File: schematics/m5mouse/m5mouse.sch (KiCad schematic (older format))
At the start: 52 parts, among them IC1 LM3940IMP-3.3_NOPB, J1 Conn_01x02, J2 M-BUS, J3 SWD, J6 Conn_01x03, J7 Conn_01x06, J8 Conn_01x06, SW1 SW_SPDT, SW2 SW_Push, U1 TPS562200, U2 STM32F405RGTx, Y1 8MHz, Y2 32.768kHz

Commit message: Fix path
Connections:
- net GND: no longer C15.1, C16.1, C17.1, U2.12 (VSSA)
- net GPIO10: now also U2.50 (PA15); no longer U2.34 (PB13)
- new net GNDA: C15.1, C16.1, C17.1, U2.12 (VSSA)
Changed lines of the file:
@@
 Wire Wire Line
 	12200 7200 12200 7300
-Wire Wire Line
-	12200 7300 12300 7300
-Wire Wire Line
-	12300 7300 12300 7200
-Wire Wire Line
-	12300 7300 12400 7300
-Wire Wire Line
-	12400 7300 12400 7200
-Connection ~ 12300 7300
-Wire Wire Line
-	12300 7300 12300 7400
 $Comp
 L Device:C C11
@@
 	13450 3100 13450 3200
 Connection ~ 13150 3100
-$Comp
-L power:GND #PWR0108
-U 1 1 5EECB65E
-P 13850 3200
-F 0 "#PWR0108" H 13850 2950 50  0001 C CNN
-F 1 "GND" H 13855 3027 50  0000 C CNN
-F 2 "" H 13850 3200 50  0001 C CNN
-F 3 "" H 13850 3200 50  0001 C CNN
-	1    13850 3200
-	1    0    0    -1
-$EndComp
 Wire Wire Line
 	13450 3100 13850 3100
@@
 Text GLabel 13250 5600 2    50   Output ~ 0
 GPIO3
-Text GLabel 9550 9400 0    50   Input ~ 0
+Text GLabel 9550 9100 0    50   Input ~ 0
 GPIO5
-Text GLabel 9550 9250 0    50   Input ~ 0
+Text GLabel 9550 8950 0    50   Input ~ 0
 GPIO4
-Text GLabel 9550 9100 0    50   Input ~ 0
+Text GLabel 9550 9400 0    50   Input ~ 0
 GPIO3
-Text GLabel 9550 8950 0    50   Input ~ 0
+Text GLabel 9550 9250 0    50   Input ~ 0
 GPIO2
 Text GLabel 11500 8950 2    50   Output ~ 0
@@
 Wire Wire Line
 	9350 2300 9350 2250
-Text GLabel 13250 6800 2    50   Output ~ 0
+Text GLabel 13250 5300 2    50   Output ~ 0
 GPIO10
 Text GLabel 9550 6750 2    50   Input ~ 0
@@
 Wire Wire Line
 	13000 6700 13250 6700
-Wire Wire Line
-	13250 6800 13000 6800
-$Comp
-L power:GNDA #PWR028
-U 1 1 5F5519D3
-P 12300 7500
-F 0 "#PWR028" H 12300 7250 50  0001 C CNN
-F 1 "GNDA" H 12305 7327 50  0000 C CNN
-F 2 "" H 12300 7500 50  0001 C CNN
-F 3 "" H 12300 7500 50  0001 C CNN
-	1    12300 7500
-	1    0    0    -1
-$EndComp
-$Comp
-L power:GND #PWR027
-U 1 1 5F551FD9
-P 11900 7500
-F 0 "#PWR027" H 11900 7250 50  0001 C CNN
-F 1 "GND" H 11905 7327 50  0000 C CNN
-F 2 "" H 11900 7500 50  0001 C CNN
-F 3 "" H 11900 7500 50  0001 C CNN
-	1    11900 7500
-	1    0    0    -1
-$EndComp
-Wire Wire Line
-	11900 7500 11900 7400
-Wire Wire Line
-	11900 7400 12300 7400
-Connection ~ 12300 7400
-Wire Wire Line
-	12300 7400 12300 7500
 $Sheet
 S 13400 7850 1050 650
@@
 Text GLabel 13250 4200 2    50   Output ~ 0
 GPIO11
-NoConn ~ 13000 5300
+NoConn ~ 13000 6800
 Text GLabel 11350 6700 0    50   Output ~ 0
 SPI1_CS
@@
 	14200 3600 15000 3600
 NoConn ~ 11600 6600
+Wire Wire Line
+	12300 7200 12300 7300
+Wire Wire Line
+	12300 7300 12200 7300
+$Comp
+L power:GNDA #PWR0108
+U 1 1 5F55198E
+P 13850 3200
+F 0 "#PWR0108" H 13850 2950 50  0001 C CNN
+F 1 "GNDA" H 13855 3027 50  0000 C CNN
+F 2 "" H 13850 3200 50  0001 C CNN
+F 3 "" H 13850 3200 50  0001 C CNN
+	1    13850 3200
+	1    0    0    -1
+$EndComp
+$Comp
+L power:GNDA #PWR028
+U 1 1 5F5519D3
+P 12400 7500
+F 0 "#PWR028" H 12400 7250 50  0001 C CNN
+F 1 "GNDA" H 12405 7327 50  0000 C CNN
+F 2 "" H 12400 7500 50  0001 C CNN
+F 3 "" H 12400 7500 50  0001 C CNN
+	1    12400 7500
+	1    0    0    -1
+$EndComp
+Connection ~ 12200 7300
+$Comp
+L power:GND #PWR027
+U 1 1 5F551FD9
+P 11900 7500
+F 0 "#PWR027" H 11900 7250 50  0001 C CNN
+F 1 "GND" H 11905 7327 50  0000 C CNN
+F 2 "" H 11900 7500 50  0001 C CNN
+F 3 "" H 11900 7500 50  0001 C CNN
+	1    11900 7500
+	1    0    0    -1
+$EndComp
+Wire Wire Line
+	11900 7300 11900 7500
+Wire Wire Line
+	12200 7300 11900 7300
+Wire Wire Line
+	12400 7200 12400 7500
+$Comp
+L power:GNDA #PWR0136
+U 1 1 5F651608
+P 3500 1350
+F 0 "#PWR0136" H 3500 1100 50  0001 C CNN
+F 1 "GNDA" H 3505 1177 50  0000 C CNN
+F 2 "" H 3500 1350 50  0001 C CNN
+F 3 "" H 3500 1350 50  0001 C CNN
+	1    3500 1350
+	1    0    0    -1
+$EndComp
+$Comp
+L power:PWR_FLAG #FLG0103
+U 1 1 5F666704
+P 3500 1150
+F 0 "#FLG0103" H 3500 1225 50  0001 C CNN
+F 1 "PWR_FLAG" H 3500 1323 50  0000 C CNN
+F 2 "" H 3500 1150 50  0001 C CNN
+F 3 "~" H 3500 1150 50  0001 C CNN
+	1    3500 1150
+	1    0    0    -1
+$EndComp
+Wire Wire Line
+	3500 1150 3500 1350
+Wire Wire Line
+	13000 5300 13250 5300
 $EndSCHEMATC

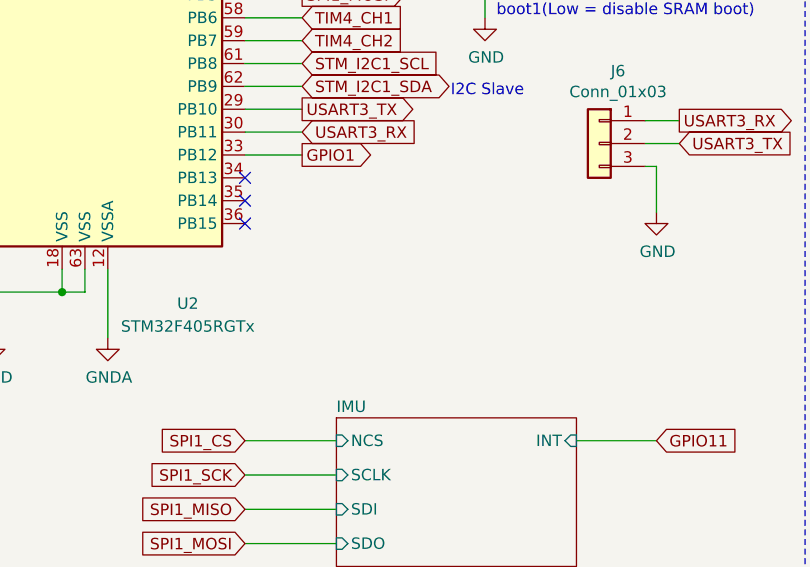
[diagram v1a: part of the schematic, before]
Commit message: Connect GNDA and GND via ferrite bead
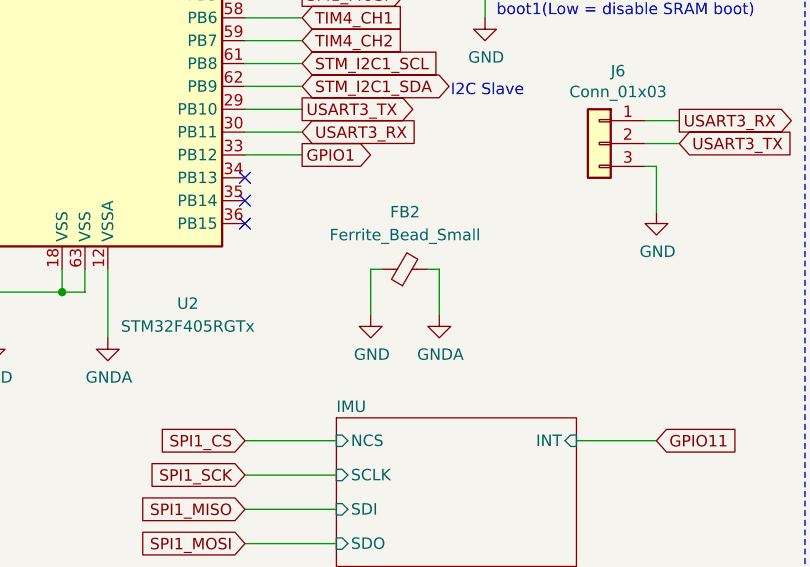
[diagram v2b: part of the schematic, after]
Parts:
- added FB2: Ferrite_Bead_Small, Resistor_SMD:R_0603_1608Metric, symbol Device:Ferrite_Bead_Small
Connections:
- net GND: now also FB2.1
- net GNDA: now also FB2.2
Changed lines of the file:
@@
 	1550 4650 1600 4650
 $Comp
-L MCU_ST_STM32F4:STM32F405RGTx U2
-U 1 1 5ED1928B
-P 12300 5400
-F 0 "U2" H 12750 3450 50  0000 C CNN
-F 1 "STM32F405RGTx" H 12750 3350 50  0000 C CNN
-F 2 "Package_QFP:LQFP-64_10x10mm_P0.5mm" H 11700 3700 50  0001 R CNN
-F 3 "http://www.st.com/st-web-ui/static/active/en/resource/technical/document/datasheet/DM00037051.pdf" H 12300 5400 50  0001 C CNN
-	1    12300 5400
-	1    0    0    -1
-$EndComp
-$Comp
 L Regulator_Switching:TPS562200 U1
 U 1 1 5ED6693A
@@
 L power:GNDA #PWR028
 U 1 1 5F5519D3
-P 12400 7500
-F 0 "#PWR028" H 12400 7250 50  0001 C CNN
-F 1 "GNDA" H 12405 7327 50  0000 C CNN
-F 2 "" H 12400 7500 50  0001 C CNN
-F 3 "" H 12400 7500 50  0001 C CNN
-	1    12400 7500
+P 13850 7400
+F 0 "#PWR028" H 13850 7150 50  0001 C CNN
+F 1 "GNDA" H 13855 7227 50  0000 C CNN
+F 2 "" H 13850 7400 50  0001 C CNN
+F 3 "" H 13850 7400 50  0001 C CNN
+	1    13850 7400
 	1    0    0    -1
 $EndComp
@@
 $EndComp
 Wire Wire Line
-	11900 7300 11900 7500
-Wire Wire Line
 	12200 7300 11900 7300
-Wire Wire Line
-	12400 7200 12400 7500
 $Comp
 L power:GNDA #PWR0136
@@
 Wire Wire Line
 	13000 5300 13250 5300
+Wire Wire Line
+	11900 7300 11900 7500
+$Comp
+L MCU_ST_STM32F4:STM32F405RGTx U2
+U 1 1 5ED1928B
+P 12300 5400
+F 0 "U2" H 12750 3450 50  0000 C CNN
+F 1 "STM32F405RGTx" H 12750 3350 50  0000 C CNN
+F 2 "Package_QFP:LQFP-64_10x10mm_P0.5mm" H 11700 3700 50  0001 R CNN
+F 3 "http://www.st.com/st-web-ui/static/active/en/resource/technical/document/datasheet/DM00037051.pdf" H 12300 5400 50  0001 C CNN
+	1    12300 5400
+	1    0    0    -1
+$EndComp
+Wire Wire Line
+	13850 7200 13850 7400
+Wire Wire Line
+	13800 7200 13850 7200
+$Comp
+L power:GNDA #PWR?
+U 1 1 5F7205BA
+P 12400 7500
+F 0 "#PWR?" H 12400 7250 50  0001 C CNN
+F 1 "GNDA" H 12405 7327 50  0000 C CNN
+F 2 "" H 12400 7500 50  0001 C CNN
+F 3 "" H 12400 7500 50  0001 C CNN
+	1    12400 7500
+	1    0    0    -1
+$EndComp
+Wire Wire Line
+	12400 7200 12400 7500
+$Comp
+L Device:Ferrite_Bead_Small FB2
+U 1 1 5F593E8C
+P 13700 7200
+F 0 "FB2" V 13950 7200 50  0000 C CNN
+F 1 "Ferrite_Bead_Small" V 13850 7200 50  0000 C CNN
+F 2 "Resistor_SMD:R_0603_1608Metric" V 13630 7200 50  0001 C CNN
+F 3 "~" H 13700 7200 50  0001 C CNN
+	1    13700 7200
+	0    -1   -1   0
+$EndComp
+$Comp
+L power:GND #PWR?
+U 1 1 5F78F290
+P 13550 7400
+F 0 "#PWR?" H 13550 7150 50  0001 C CNN
+F 1 "GND" H 13555 7227 50  0000 C CNN
+F 2 "" H 13550 7400 50  0001 C CNN
+F 3 "" H 13550 7400 50  0001 C CNN
+	1    13550 7400
+	1    0    0    -1
+$EndComp
+Wire Wire Line
+	13600 7200 13550 7200
+Wire Wire Line
+	13550 7200 13550 7400
 $EndSCHEMATC
